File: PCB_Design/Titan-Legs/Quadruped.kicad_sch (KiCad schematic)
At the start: 46 parts, among them IC1 TPS54260DGQR, IC2 CP2102, J1 TYPE-C-31-M-12, P1 282837-2, SW1 SW_Push, SW2 SW_Push, T1 BC847, T2 BC847, U1 ESP32-S3-WROOM-1, U4 AMS1117-3.3

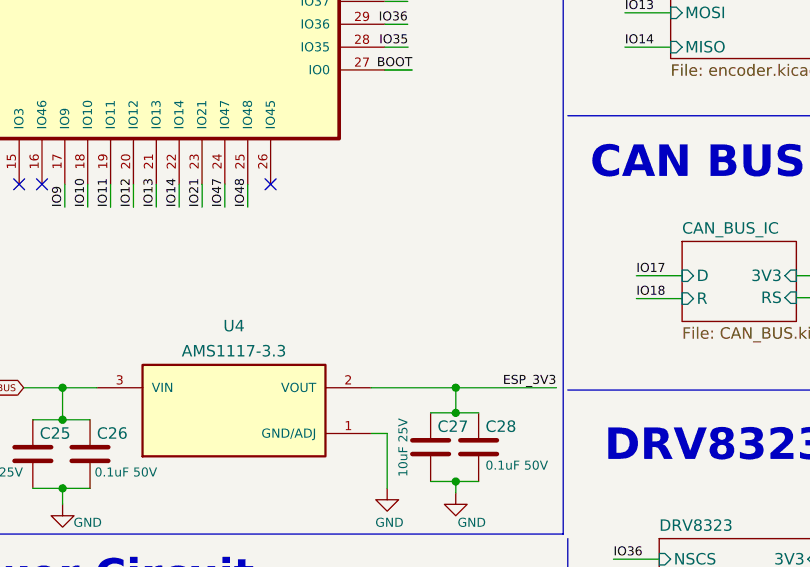
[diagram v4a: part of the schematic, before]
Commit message: Merged the silkscreen MA,MB,MC and added vias in shunt resistors
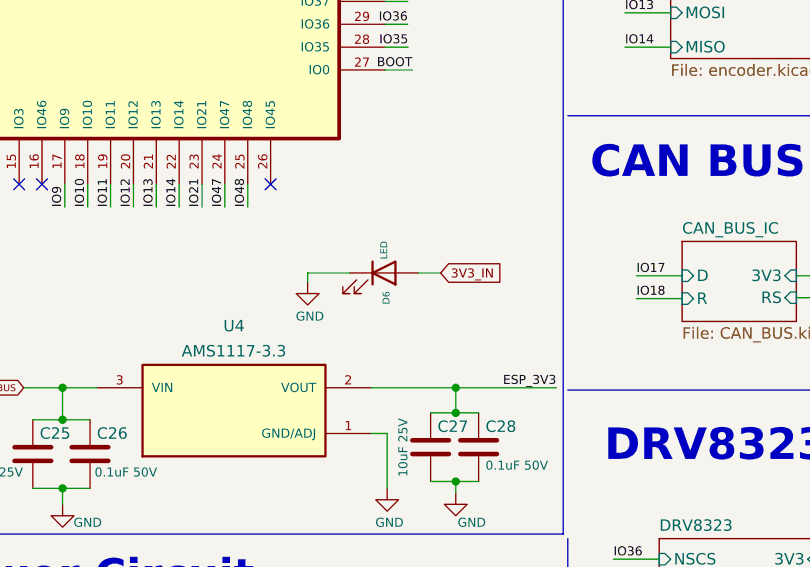
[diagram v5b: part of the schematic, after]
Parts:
- added D6: LED, LED_SMD:LED_0402_1005Metric, symbol Device:LED
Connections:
- net 3V3_IN: now also D6.2 (A)
- net GND: now also D6.1 (K)
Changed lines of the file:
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@@
+    (stroke (width 0) (type default) (color 0 0 0 0))
+  )
+  (wire (pts (xy 81.5848 105.1052) (xy 86.2584 105.1052))
     (stroke (width 0) (type default) (color 0 0 0 0))
   )
@@
     (stroke (width 0) (type default) (color 0 0 0 0))
   )
+  (wire (pts (xy 93.8784 105.1052) (xy 96.3676 105.1052))
+    (stroke (width 0) (type default) (color 0 0 0 0))
+  )
   (wire (pts (xy 140.8684 189.0776) (xy 140.8684 186.2836))
     (stroke (width 0) (type default) (color 0 0 0 0))
@@
   )
   (wire (pts (xy 219.71 143.51) (xy 226.06 143.51))
+    (stroke (width 0) (type default) (color 0 0 0 0))
+  )
+  (wire (pts (xy 81.5848 105.1052) (xy 81.5848 106.1212))
     (stroke (width 0) (type default) (color 0 0 0 0))
   )
@@
       (effects (font (size 1 1)) (justify right) hide)
     )
+  )
+  (global_label "3V3_IN" (shape input) (at 96.3676 105.1052 0) (fields_autoplaced)
+    (effects (font (size 1 1)) (justify left))
+    (property "Intersheet References" "${INTERSHEET_REFS}" (id 0) (at 103.3152 105.1677 0)
+      (effects (font (size 1 1)) (justify left) hide)
+    )
+  )
+  (symbol (lib_id "power:GND") (at 81.5848 106.1212 0) (unit 1)
+    (in_bom yes) (on_board yes)
+    (property "Reference" "#PWR035" (id 0) (at 81.5848 112.4712 0)
+      (effects (font (size 1.27 1.27)) hide)
+    )
+    (property "Value" "GND" (id 1) (at 81.8388 109.9312 0)
+      (effects (font (size 1 1)))
+    )
+    (property "Footprint" "" (id 2) (at 81.5848 106.1212 0)
+      (effects (font (size 1.27 1.27)) hide)
+    )
+    (property "Datasheet" "" (id 3) (at 81.5848 106.1212 0)
+      (effects (font (size 1.27 1.27)) hide)
+    )
+    (pin "1")
   )
   (symbol (lib_id "Terminal_Block:282837-2") (at 148.4884 183.7436 0) (unit 1)
@@
     )
     (property "Datasheet" "~" (id 3) (at 99.06 166.37 0)
+      (effects (font (size 1.27 1.27)) hide)
+    )
+    (pin "1")
+    (pin "2")
+  )
+  (symbol (lib_id "Device:LED") (at 90.0684 105.1052 0) (unit 1)
+    (in_bom yes) (on_board yes)
+    (property "Reference" "D6" (id 0) (at 90.3224 107.1372 90)
+      (effects (font (size 0.762 0.762)) (justify right))
+    )
+    (property "Value" "LED" (id 1) (at 90.0684 101.5492 90)
+      (effects (font (size 0.762 0.762)) (justify right))
+    )
+    (property "Footprint" "LED_SMD:LED_0402_1005Metric" (id 2) (at 90.0684 105.1052 0)
+      (effects (font (size 1.27 1.27)) hide)
+    )
+    (property "Datasheet" "~" (id 3) (at 90.0684 105.1052 0)
       (effects (font (size 1.27 1.27)) hide)
     )
@@
       (reference "#PWR034") (unit 1) (value "GND") (footprint "")
     )
-    (path "/983771df-a9d8-4c95-b2f8-7263116735ed/0f6a5dcb-5d31-4f0c-8485-9ccff795eda8"
-      (reference "#PWR038") (unit 1) (value "GND") (footprint "")
+    (path "/03392147-12c6-4ee1-9fc3-368f0528ab17"
+      (reference "#PWR035") (unit 1) (value "GND") (footprint "")
     )
     (path "/af4aaf40-49eb-45e6-8872-03a32e06c75b"
@@
       (reference "C17") (unit 1) (value "0.1uF") (footprint "Capacitor_SMD:C_0603_1608Metric")
     )
-    (path "/983771df-a9d8-4c95-b2f8-7263116735ed/3a91d955-b555-49b1-b924-046e3e4bd045"
-      (reference "C18") (unit 1) (value "0.1uF") (footprint "Capacitor_SMD:C_0603_1608Metric")
-    )
     (path "/983771df-a9d8-4c95-b2f8-7263116735ed/6afbdf4b-afc5-4f11-9f16-bcebe7b5864b"
       (reference "C19") (unit 1) (value "0.1uF 6.3V") (footprint "Capacitor_SMD:C_0603_1608Metric")
@@
       (reference "D5") (unit 1) (value "LED") (footprint "LED_SMD:LED_0402_1005Metric")
     )
+    (path "/71f39d0e-9797-49e8-b383-41e330f8d426"
+      (reference "D6") (unit 1) (value "LED") (footprint "LED_SMD:LED_0402_1005Metric")
+    )
     (path "/fddf2939-6581-4168-83e6-bfc5e62b7a8a"

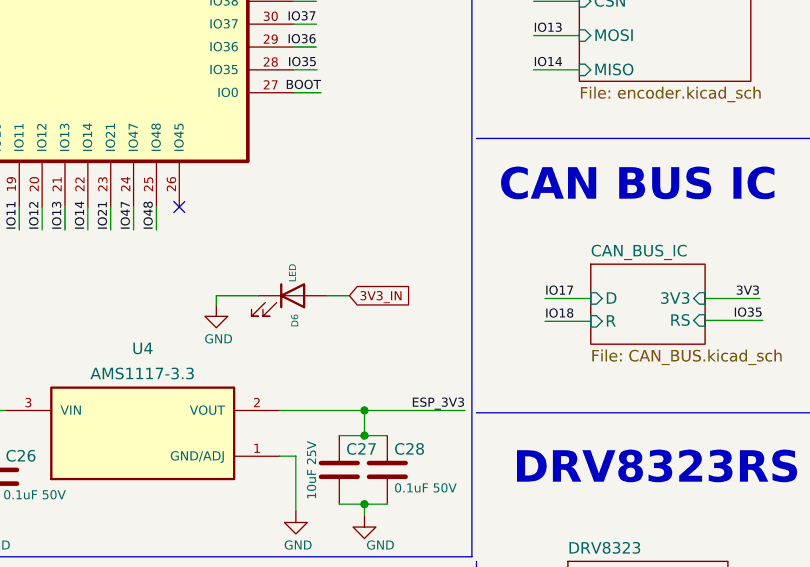
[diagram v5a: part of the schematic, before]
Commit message: Merged the silkscreen MA,MB,MC and added more vias in shunt resistors
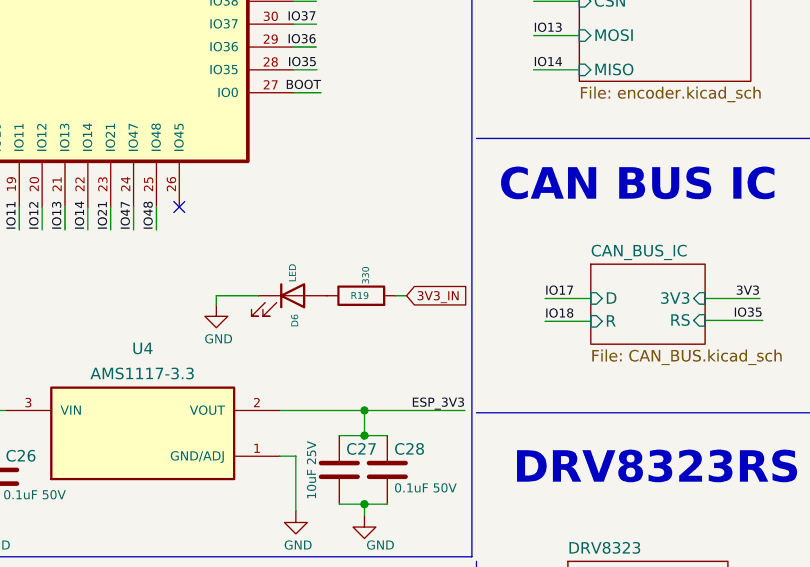
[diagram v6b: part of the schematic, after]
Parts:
- added R19: 330, Resistor_SMD:R_0402_1005Metric, symbol Device:R
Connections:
- net 3V3_IN: now also R19.2; no longer D6.2 (A)
- new net: D6.2 (A), R19.1
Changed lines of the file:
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@@
-    (stroke (width 0) (type default) (color 0 0 0 0))
-  )
-  (wire (pts (xy 93.8784 105.1052) (xy 96.3676 105.1052))
     (stroke (width 0) (type default) (color 0 0 0 0))
   )
@@
   )
   (wire (pts (xy 168.402 54.102) (xy 168.402 43.942))
+    (stroke (width 0) (type default) (color 0 0 0 0))
+  )
+  (wire (pts (xy 101.4984 105.1052) (xy 102.7176 105.1052))
     (stroke (width 0) (type default) (color 0 0 0 0))
   )
@@
     )
   )
-  (global_label "3V3_IN" (shape input) (at 96.3676 105.1052 0) (fields_autoplaced)
+  (global_label "3V3_IN" (shape input) (at 102.7176 105.1052 0) (fields_autoplaced)
     (effects (font (size 1 1)) (justify left))
-    (property "Intersheet References" "${INTERSHEET_REFS}" (id 0) (at 103.3152 105.1677 0)
+    (property "Intersheet References" "${INTERSHEET_REFS}" (id 0) (at 109.6652 105.1677 0)
       (effects (font (size 1 1)) (justify left) hide)
     )
@@
     )
     (property "Datasheet" "~" (id 3) (at 172.974 84.582 0)
+      (effects (font (size 1.27 1.27)) hide)
+    )
+    (pin "1")
+    (pin "2")
+  )
+  (symbol (lib_id "Device:R") (at 97.6884 105.1052 90) (unit 1)
+    (in_bom yes) (on_board yes)
+    (property "Reference" "R19" (id 0) (at 98.552 105.1052 90)
+      (effects (font (size 0.762 0.762)) (justify left))
+    )
+    (property "Value" "330" (id 1) (at 98.1964 103.8352 0)
+      (effects (font (size 0.762 0.762)) (justify left))
+    )
+    (property "Footprint" "Resistor_SMD:R_0402_1005Metric" (id 2) (at 97.6884 106.8832 90)
+      (effects (font (size 1.27 1.27)) hide)
+    )
+    (property "Datasheet" "~" (id 3) (at 97.6884 105.1052 0)
       (effects (font (size 1.27 1.27)) hide)
     )
@@
       (reference "R18") (unit 1) (value "10k") (footprint "Resistor_SMD:R_0402_1005Metric")
     )
+    (path "/67baaf70-7dfd-4b9b-86cc-b107697fb088"
+      (reference "R19") (unit 1) (value "330") (footprint "Resistor_SMD:R_0402_1005Metric")
+    )
     (path "/eb4a6687-cba5-448e-acce-d7bcbebf069b"

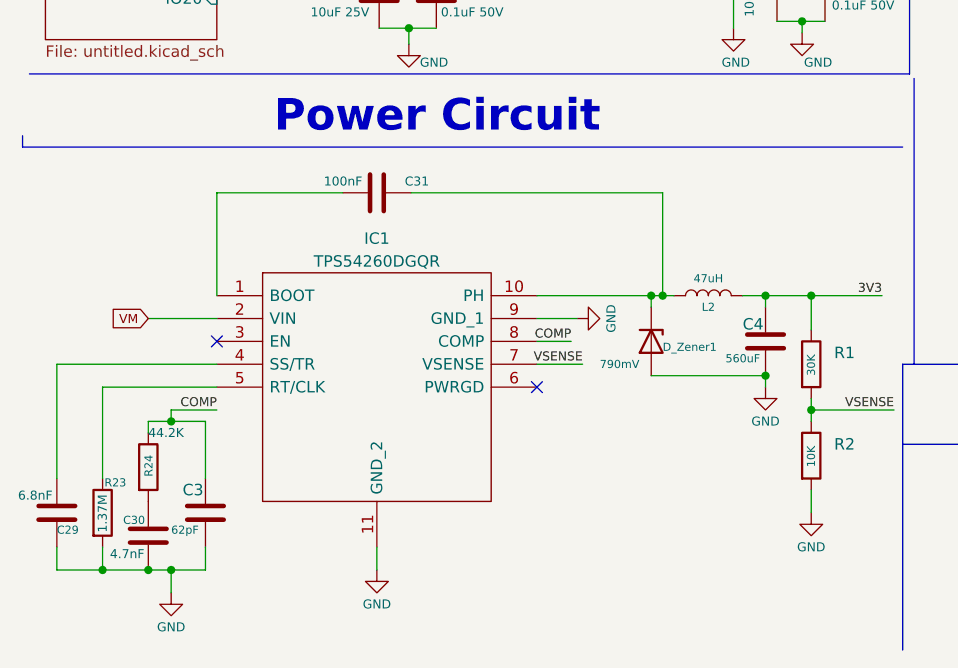
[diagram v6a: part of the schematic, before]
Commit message: Added Electrolytic Capacitor for TPS54260 and resisotrs for EN pin
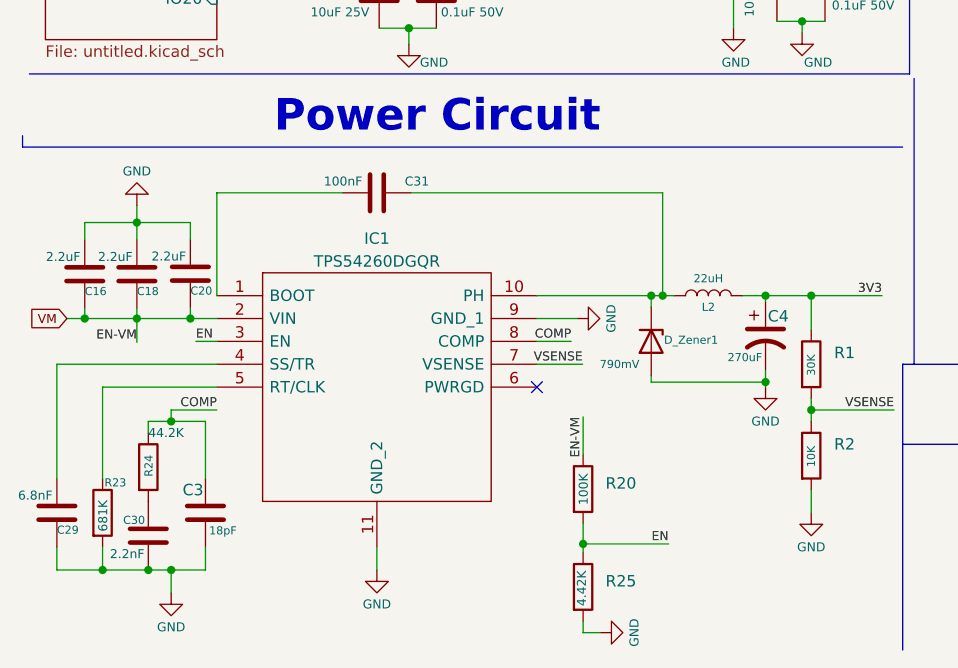
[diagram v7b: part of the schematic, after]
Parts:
- removed C4: 560uF, Capacitor_SMD:C_0603_1608Metric, symbol Device:C
- added C16, C18, C20: 2.2uF, Capacitor_SMD:C_0603_1608Metric, symbol Device:C
- added C4: 270uF, Capacitor_SMD:CP_Elec_8x10, symbol Device:C_Polarized_US
- added R20: 100K, Resistor_SMD:R_0603_1608Metric, symbol Device:R
- added R25: 4.42K, Resistor_SMD:R_0603_1608Metric, symbol Device:R
- C3: value 62pF -> 18pF
- C30: value 4.7nF -> 2.2nF
- L2: value 47uH -> 22uH
- R23: value 1.37M -> 681K
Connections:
- net 3V3_IN: now also C4.1
- net EN: now also IC1.3 (EN), R20.2, R25.1
- net GND: now also C16.1, C18.1, C20.1, C4.2, R25.2
- net VM: now also C16.2, C18.2, C20.2, R20.1
- no-connect marks 24 -> 23

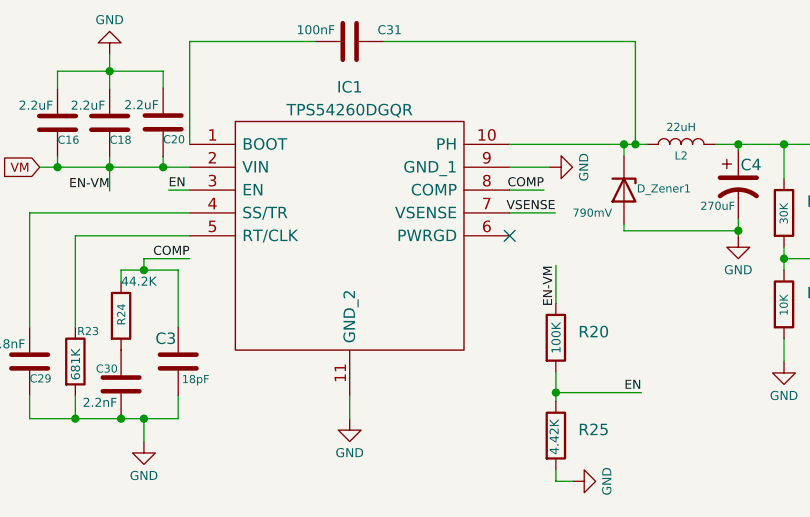
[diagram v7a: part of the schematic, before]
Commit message: Added Electrolytic Capacitor and moved AMS1117 to B.Cu
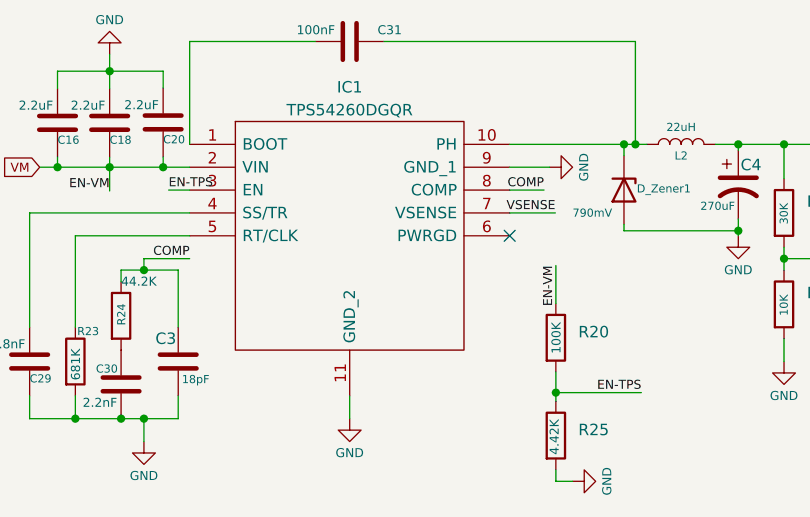
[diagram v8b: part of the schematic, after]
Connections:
- net EN: no longer IC1.3 (EN), R20.2, R25.1
- new net EN-TPS: IC1.3 (EN), R20.2, R25.1
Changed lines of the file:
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@@
     (effects (font (size 1 1)) (justify right bottom))
   )
-  (label "EN" (at 83.2104 186.3344 180)
+  (label "EN-TPS" (at 83.2104 186.3344 180)
     (effects (font (size 1 1)) (justify right bottom))
   )
@@
     (effects (font (size 1 1)) (justify left bottom))
   )
-  (label "EN" (at 30.6832 163.83 0)
+  (label "EN-TPS" (at 30.6832 163.83 0)
     (effects (font (size 1 1)) (justify left bottom))
   )
@@
       (reference "#PWR019") (unit 1) (value "GND") (footprint "")
     )
-    (path "/ee34e5ea-1d84-4f7f-ac75-7ea4a480f5c1/8fcec146-4996-4a7f-806d-e42bcad37ef9"
-      (reference "#PWR020") (unit 1) (value "GND") (footprint "")
-    )
-    (path "/ee34e5ea-1d84-4f7f-ac75-7ea4a480f5c1/8b08e164-bdfa-4d52-9727-96a841b79633"
-      (reference "#PWR021") (unit 1) (value "GND") (footprint "")
-    )
-    (path "/ee34e5ea-1d84-4f7f-ac75-7ea4a480f5c1/cc2b53fc-ccbc-4fdc-9f77-f456f85e910b"
-      (reference "#PWR022") (unit 1) (value "GND") (footprint "")
-    )
-    (path "/eb34d206-56ca-44ca-9e9b-c8513ecb240f/798dc8a4-29e6-482a-b9dd-86fc0253ab17"
-      (reference "#PWR023") (unit 1) (value "GND") (footprint "")
-    )
-    (path "/eb34d206-56ca-44ca-9e9b-c8513ecb240f/6a262425-bd38-472f-897e-f38659e402e1"
-      (reference "#PWR024") (unit 1) (value "GND") (footprint "")
-    )
-    (path "/eb34d206-56ca-44ca-9e9b-c8513ecb240f/1d5ae576-7b29-4a94-89a3-8ef017a1da93"
-      (reference "#PWR025") (unit 1) (value "GND") (footprint "")
-    )
     (path "/983771df-a9d8-4c95-b2f8-7263116735ed/0911e540-b0e8-47f1-8852-df8433bb20c6"
       (reference "#PWR026") (unit 1) (value "GND") (footprint "")
@@
       (reference "#PWR031") (unit 1) (value "GND") (footprint "")
     )
-    (path "/b23984b5-9f54-4356-8a16-c3212b50a2a0/d3b545ad-427d-4143-b793-c05764b9bf4b"
-      (reference "#PWR032") (unit 1) (value "GND") (footprint "")
-    )
     (path "/983771df-a9d8-4c95-b2f8-7263116735ed/07378506-2595-4739-920b-b13951bf4ab8"
       (reference "#PWR033") (unit 1) (value "GND") (footprint "")
@@
       (reference "C7") (unit 1) (value "1uF 16V") (footprint "Capacitor_SMD:C_0603_1608Metric")
     )
-    (path "/ee34e5ea-1d84-4f7f-ac75-7ea4a480f5c1/559c6654-f981-4d14-8402-9f71f52d20ae"
-      (reference "C8") (unit 1) (value "0.1uF") (footprint "Capacitor_SMD:C_0603_1608Metric")
-    )
-    (path "/eb34d206-56ca-44ca-9e9b-c8513ecb240f/6bb71b48-649c-440c-89c8-a24330a88c6e"
-      (reference "C9") (unit 1) (value "0.1uF") (footprint "Capacitor_SMD:C_0603_1608Metric")
-    )
     (path "/983771df-a9d8-4c95-b2f8-7263116735ed/408e41b9-98f7-4b37-bc88-549c410f6195"
       (reference "C10") (unit 1) (value "1uF") (footprint "Capacitor_SMD:C_0603_1608Metric")
@@
       (reference "D_Zener1") (unit 1) (value "790mV") (footprint "Diode_SMD:D_SMB")
     )
-    (path "/b23984b5-9f54-4356-8a16-c3212b50a2a0/168619e9-c663-4616-a034-eddd892637d1"
-      (reference "H1") (unit 1) (value "MountingHole") (footprint "MountingHole:MountingHole_4mm")
-    )
-    (path "/b23984b5-9f54-4356-8a16-c3212b50a2a0/ffd87500-2450-4967-8daa-c9eb5219b85c"
-      (reference "H2") (unit 1) (value "MountingHole") (footprint "MountingHole:MountingHole_4mm")
-    )
-    (path "/b23984b5-9f54-4356-8a16-c3212b50a2a0/5c804850-8c78-40df-876a-8af32ee895b8"
-      (reference "H3") (unit 1) (value "MountingHole") (footprint "MountingHole:MountingHole_4mm")
-    )
-    (path "/b23984b5-9f54-4356-8a16-c3212b50a2a0/b3df3f30-0ef0-4520-bdff-e49e041fe09b"
-      (reference "H4") (unit 1) (value "MountingHole") (footprint "MountingHole:MountingHole_4mm")
-    )
     (path "/eb4f4b08-64cf-4eb0-bd2e-4a4095f865c4"
       (reference "IC1") (unit 1) (value "TPS54260DGQR") (footprint "Buck Converter:IC_XTR111AIDGQR")
@@
       (reference "P1") (unit 1) (value "282837-2") (footprint "TerminalBlock:TerminalBlock_bornier-2_P5.08mm")
     )
-    (path "/eb34d206-56ca-44ca-9e9b-c8513ecb240f/ea455ca0-0229-48d6-9bd5-db8ca12e58cd"
-      (reference "P2") (unit 1) (value "282837-2") (footprint "TerminalBlock:TerminalBlock_bornier-2_P5.08mm")
-    )
     (path "/983771df-a9d8-4c95-b2f8-7263116735ed/83c31b50-9630-47ba-8a3f-cda527279593"
       (reference "Q1") (unit 1) (value "BSC031N06NS3GATMA1") (footprint "BSC_Mosfets:PG-TDSON-8_1")
@@
       (reference "R9") (unit 1) (value "10K") (footprint "Resistor_SMD:R_0402_1005Metric")
     )
-    (path "/b23984b5-9f54-4356-8a16-c3212b50a2a0/ca410c7b-44b9-4164-b021-bbf1896d7bc4"
-      (reference "R10") (unit 1) (value "4.7K") (footprint "Resistor_SMD:R_0603_1608Metric")
-    )
-    (path "/ee34e5ea-1d84-4f7f-ac75-7ea4a480f5c1/d1a6be26-f263-4b0c-8aa1-f0987ad122ce"
-      (reference "R11") (unit 1) (value "10K") (footprint "Resistor_SMD:R_0603_1608Metric")
-    )
     (path "/68a33b1b-c5a4-46e0-8867-0ecbab278f47"
       (reference "R12") (unit 1) (value "5.1k") (footprint "Resistor_SMD:R_0402_1005Metric")
     )
-    (path "/eb34d206-56ca-44ca-9e9b-c8513ecb240f/6fef41bf-697e-4d5b-9684-0d857b9965a7"
-      (reference "R13") (unit 1) (value "10K") (footprint "Resistor_SMD:R_0402_1005Metric")
-    )
     (path "/983771df-a9d8-4c95-b2f8-7263116735ed/1616499b-6a69-425e-b8fa-e342d6d49a89"
       (reference "R14") (unit 1) (value "0.5m") (footprint "Resistor_6.4mm_3.2mm_1.2mm_pads:R_0.5m")
@@
       (reference "U1") (unit 1) (value "ESP32-S3-WROOM-1") (footprint "RF_Module:ESP32-S3-WROOM-1")
     )
-    (path "/ee34e5ea-1d84-4f7f-ac75-7ea4a480f5c1/124cb5ee-9827-4498-8534-b6cd5d21b22f"
-      (reference "U2") (unit 1) (value "AS5047P-ATSM") (footprint "ENCODER:SOP65P640X120-14N")
-    )
-    (path "/eb34d206-56ca-44ca-9e9b-c8513ecb240f/8593b77f-2b7e-4641-ac14-633906214e4b"
-      (reference "U3") (unit 1) (value "SN65HVD230DR") (footprint "CAN-BUS-IC:SOIC127P599X175-8N")
-    )
     (path "/0d27049a-3ba4-4cf7-af8a-47d969341c74"
       (reference "U4") (unit 1) (value "AMS1117-3.3") (footprint "AMS1117-3:SOT229P700X180-4N")
     )
-    (path "/b23984b5-9f54-4356-8a16-c3212b50a2a0/dcf18123-7947-4cff-84e3-a1720bc41cab"
-      (reference "U5") (unit 1) (value "DS18S20Z+") (footprint "Temp-Sensor_DS18S20Z_:DS18S20Z_")
-    )
-  )
+  )
